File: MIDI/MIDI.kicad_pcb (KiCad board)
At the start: 2 copper layers, 85.8 x 137 mm, 136 parts, among them J1 DIN_5, J2 DIN_5, J3 DIN_5, J4 CONN_01X06, J5 CONN_01X06, SW1 SW_PUSH, SW10 SW_PUSH, SW11 SW_PUSH, SW12 SW_PUSH, SW2 SW_PUSH, SW3 SW_PUSH, SW4 SW_PUSH, SW5 SW_PUSH, SW6 SW_PUSH, SW7 SW_PUSH, SW8 SW_PUSH, SW9 SW_PUSH, U1 6N138, U2 4050, U3 40106, U4 ENCODER_w_SWITCH, U5 ENCODER_w_SWITCH, U6 ENCODER_w_SWITCH

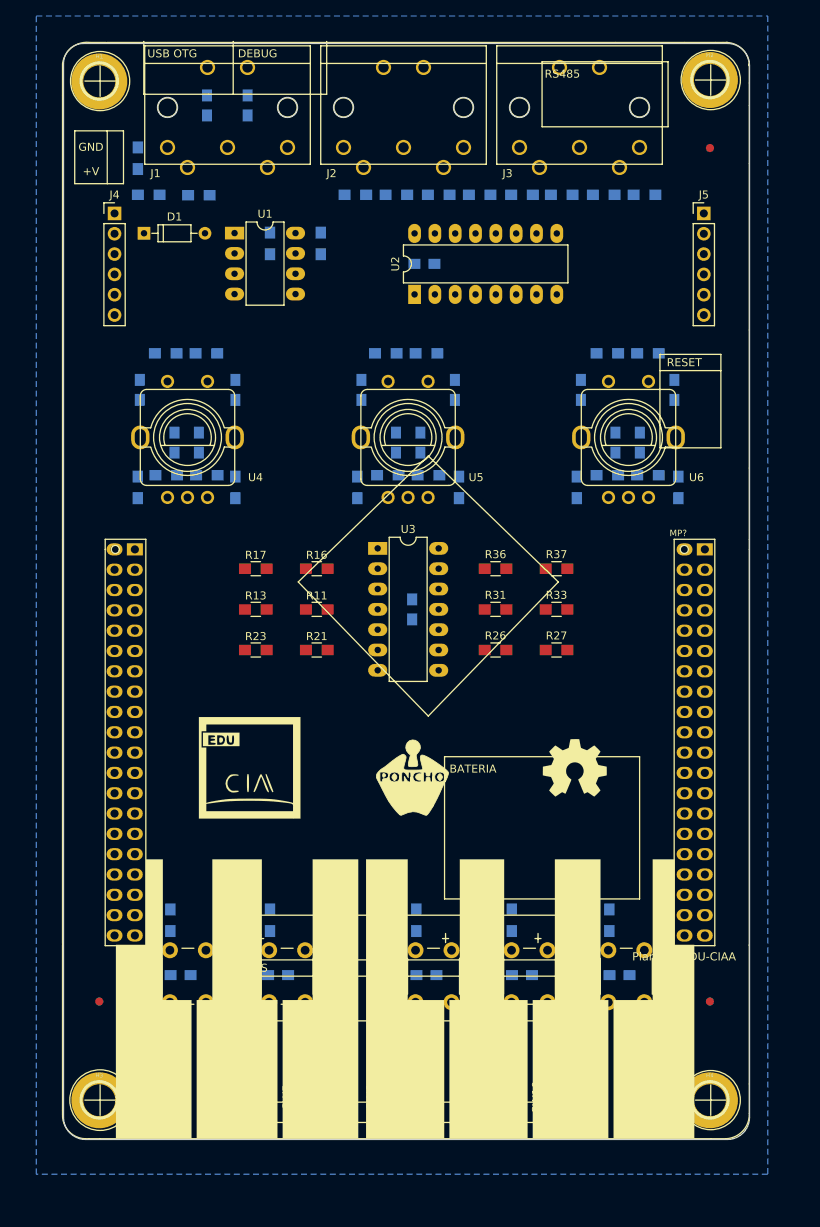
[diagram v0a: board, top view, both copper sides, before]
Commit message: Se comienza a realizar una primer iteración de ruteo
> Se trazan algunas líneas para estudiar si el placement es adecuado.
> Se realizan pequeñas modificaciones en la posición de componentes accesorios para facilitar el ruteo.
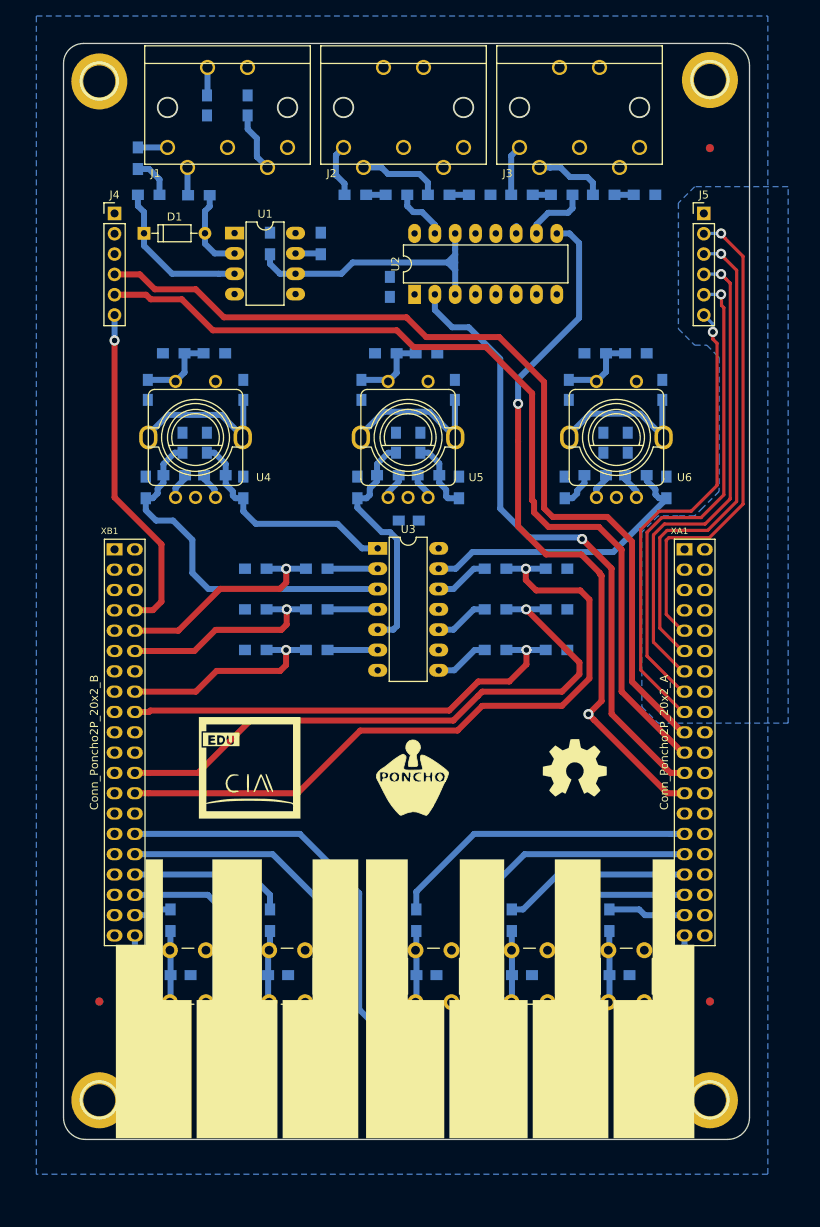
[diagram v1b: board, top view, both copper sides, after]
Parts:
- removed MP?: Plantilla_EDU-CIAA, MIDI:Plantilla_EDU-CIAA
- R11, R13, R16, R17, R21, R23, R26, R27, R31, R33, R36, R37: moved to B.Cu
- XA1, XB1: moved to F.Cu
- moved C16 11.1 mm to (84.7, 83.4), turned to 180 degrees
- moved C3 5.19 mm to (82.3, 54.2), turned to 270 degrees
- moved R47 1.78 mm to (83.6, 148.6)
- moved R51 1.78 mm to (81.8, 148.6)
- moved R53 1.78 mm to (92.2, 148.6)
- moved R49 1.75 mm to (94.0, 148.6)
- moved R29 1.51 mm to (116.9, 79.2)
- moved R30 1.51 mm to (108.0, 62.5)
- moved R32 1.51 mm to (108.0, 77.7)
- moved U6 1.51 mm to (110.6, 73.0)
- moved C12 1.51 mm to (104.7, 67.1)
- moved C13 1.51 mm to (109.0, 73.7)
- moved C14 1.51 mm to (112.0, 73.7)
- moved C15 1.51 mm to (116.3, 67.1)
- moved R28 1.51 mm to (104.2, 79.2)
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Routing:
- net /Conectores/I2C_SDA: track 0.00 -> 114.5 mm
- net /Conectores/I2C_SCL: track 0.00 -> 113.9 mm
- net /Interfaz MIDI/TX-UART: track 0.00 -> 89.0 mm, vias 0 -> 2
- net /Conectores/ENC_B2: track 0.00 -> 87.9 mm, vias 0 -> 1
- net /Interfaz MIDI/RX-UART: track 0.00 -> 78.7 mm, vias 0 -> 1
- net /Conectores/ENC_A2: track 0.00 -> 76.5 mm, vias 0 -> 1
- net /Conectores/ADC3: track 0.00 -> 61.4 mm, vias 0 -> 1
- net /Conectores/ADC1: track 0.68 -> 61.7 mm, vias 0 -> 1
- net /Conectores/ADC2: track 0.00 -> 60.9 mm, vias 0 -> 1
- net /Conectores/DAC: track 0.00 -> 60.8 mm, vias 0 -> 1
- net /Conectores/VDDA: track 0.00 -> 59.0 mm, vias 0 -> 1
- net /Conectores/ENC_B1: track 0.00 -> 58.1 mm, vias 0 -> 1
- net /Conectores/PUL5: track 0.00 -> 50.1 mm
- net Net-(C5-Pad1): track 0.00 -> 45.7 mm
- net /Conectores/PUL7: track 0.00 -> 45.0 mm
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- added copper zone on B.Cu, net /Conectores/GNDA
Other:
- net class Angosto added: clearance 0.4, trace_width 0.4, via_dia 1.27, via_drill 0.7
- net class Default: clearance 0.2 -> 0.5; trace_width 0.25 -> 0.75; via_dia 0.6 -> 1.27; via_drill 0.4 -> 0.7
- rule trace_clearance: 0.2 -> 0.5
- rule trace_min: 0.2 -> 0.3
- rule via_min_drill: 0.3 -> 0.7
- rule via_min_size: 0.4 -> 1.27
- board text added: "0,2540mm (10mils) 0,30mm 1,27mm 0,70mm MIXED MIXED HASL"
- board text added: "Grilas - Posicionamiento: - Ruteo: Valores mínimos - Pista: - Vía: - Agujero Vía: Capas - Top: - Bottom: Terminación superficial:"

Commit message: Se avanza con primera iteración de ruteo
> Se terminan de rutear conexiones para estudiar factibilidad de placement.
> Para facilitar el ruteo se realizan los siguientes cambios:
  > Se desconecta pin redundante de tact-switch's para permitir la conexión entre planos de masa.
  > Se desconectan pines del conector derecho de forma que no requieran ser ruteados a los homologos del conector izquierdo.
  > Se intercambian unidades F y D del componente 40106.
  > Se agrupan señales de los interruptores de los encoders en vez de intercalarlos con las señales de encoder, propiamente dicho, de cada uno. Se rutean a pines superiores en el conector izquierdo, mientras se desplazan las restantes señales hacia abajo.

> Se aguarda comentarios de los revisores para emprolijar, embellecer y mejorar el ruteo.
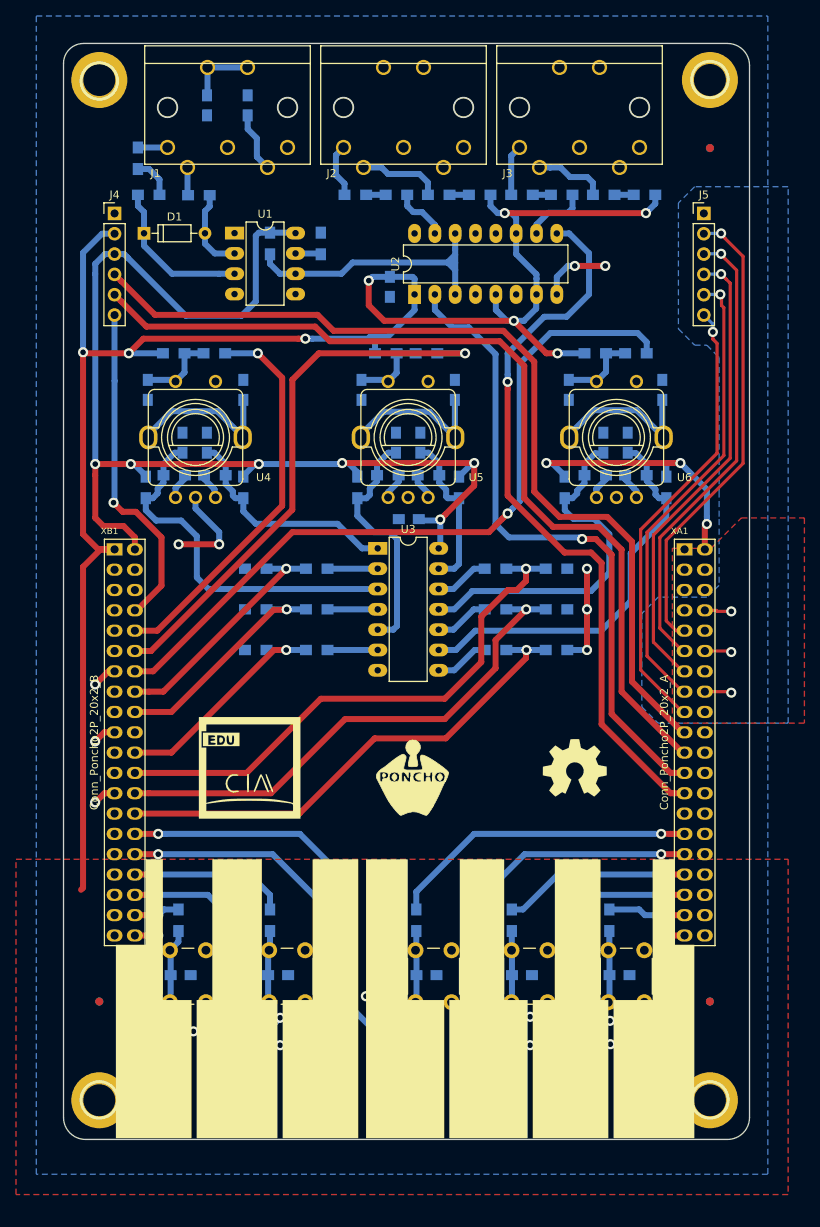
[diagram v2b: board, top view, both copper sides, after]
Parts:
- moved R26 10.2 mm to (95.5, 89.4)
- moved R27 10.2 mm to (103.1, 89.4)
- moved R36 10.2 mm to (95.5, 99.6)
- moved R37 10.2 mm to (103.1, 99.6)
- moved R43 1.00 mm to (55.9, 133.3)
- moved R39 0.51 mm to (51.6, 143.3)
- moved R42 0.20 mm to (49.8, 148.6)
- moved R53 0.20 mm to (92.0, 148.6)
- moved C16 0.18 mm to (84.7, 83.2)
- moved R50 0.15 mm to (73.3, 148.6)
- moved R51 0.15 mm to (81.6, 148.6)
- moved R61 0.15 mm to (114.7, 148.6)
- moved R55 0.10 mm to (102.3, 148.6)
- moved R41 0.05 mm to (64.5, 144.8)
- moved R40 0.05 mm to (62.5, 148.6)
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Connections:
- SW10 pad 1: Net-(C26-Pad1) -> Net-(SW10-Pad1)
- SW12 pad 1: Net-(C28-Pad1) -> Net-(SW12-Pad1)
- SW3 pad 1: Net-(C19-Pad1) -> Net-(SW3-Pad1)
- SW5 pad 1: Net-(C21-Pad1) -> Net-(SW5-Pad1)
- SW6 pad 1: Net-(C22-Pad1) -> Net-(SW6-Pad1)
- SW8 pad 1: Net-(C24-Pad1) -> Net-(SW8-Pad1)
- U3 pad 12: Net-(R36-Pad2) -> Net-(R26-Pad2)
- U3 pad 13: Net-(C14-Pad1) -> Net-(C10-Pad1)
- U3 pad 8: Net-(R26-Pad2) -> Net-(R36-Pad2)
- U3 pad 9: Net-(C10-Pad1) -> Net-(C14-Pad1)
- XA1 pad 1: +3.3V -> Net-(XA1-Pad1)
- XA1 pad 4: GND -> Net-(XA1-Pad4)
- XB1 pad 10: /Conectores/ENC_B0 -> /Conectores/ENC_SW0
- XB1 pad 12: /Conectores/ENC_A0 -> /Conectores/ENC_SW1
- XB1 pad 14: /Conectores/ENC_SW0 -> /Conectores/ENC_SW2
- XB1 pad 16: /Conectores/ENC_A1 -> /Conectores/ENC_B0
- XB1 pad 18: /Conectores/ENC_B1 -> /Conectores/ENC_A0
- XB1 pad 22: /Conectores/ENC_SW1 -> /Conectores/ENC_A1
- XB1 pad 24: /Conectores/ENC_A2 -> /Conectores/ENC_B1
- XB1 pad 26: /Conectores/ENC_B2 -> /Conectores/ENC_A2
- XB1 pad 28: /Conectores/ENC_SW2 -> /Conectores/ENC_B2
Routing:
- net +3.3V: track 0.95 -> 274.0 mm, vias 0 -> 16
- net +5V: track 0.00 -> 186.2 mm, vias 0 -> 9
- net /Conectores/ENC_SW2: track 0.00 -> 93.4 mm, vias 0 -> 1
- net /Conectores/ENC_SW1: track 0.00 -> 69.7 mm, vias 0 -> 1
- net /Conectores/ENC_SW0: track 0.00 -> 49.3 mm, vias 0 -> 1
- net GND: track 0.00 -> 42.1 mm, vias 0 -> 10
- net Net-(C13-Pad1): track 4.45 -> 45.2 mm
- net /Conectores/ENC_B2: track 87.9 -> 63.1 mm
- net Net-(C14-Pad1): track 36.6 -> 50.0 mm
- net /Conectores/ENC_A2: track 76.5 -> 65.5 mm
- net Net-(C10-Pad1): track 9.11 -> 20.1 mm
- net /Conectores/ENC_B1: track 58.1 -> 68.6 mm
- net /Conectores/GNDA: track 0.00 -> 10.1 mm, vias 0 -> 3
- net /Conectores/PUL0: track 12.5 -> 17.6 mm, vias 0 -> 1
- net Net-(C1-Pad1): track 3.52 -> 8.52 mm
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- added copper zone on F.Cu, net +3.3V
- added copper zone on F.Cu, net /Conectores/GNDA
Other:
- board text added: "0,2540mm (10mils) 0,1270/0,2540mm (5/10mils) 0,30mm 1,27mm (50mils) 0,70mm MIXED MIXED HASL"
- board text added: "Grilas - Posicionamiento: - Ruteo: Valores mínimos - Pista: - Vía: - Orificio Vía: Capas - Top: - Bottom: Terminación superficial:"
- board text removed: "0,2540mm (10mils) 0,30mm 1,27mm 0,70mm MIXED MIXED HASL"
- board text removed: "Grilas - Posicionamiento: - Ruteo: Valores mínimos - Pista: - Vía: - Agujero Vía: Capas - Top: - Bottom: Terminación superficial:"

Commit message: Correciones menores
> Se elimina nombre de componentes ( tiras de pines ) de la capa de serigrafía.
> Se realizan correciones menores al ruteo y se agregan vías para conectar plano de masa en capa bottom y conector derecho en capa front.
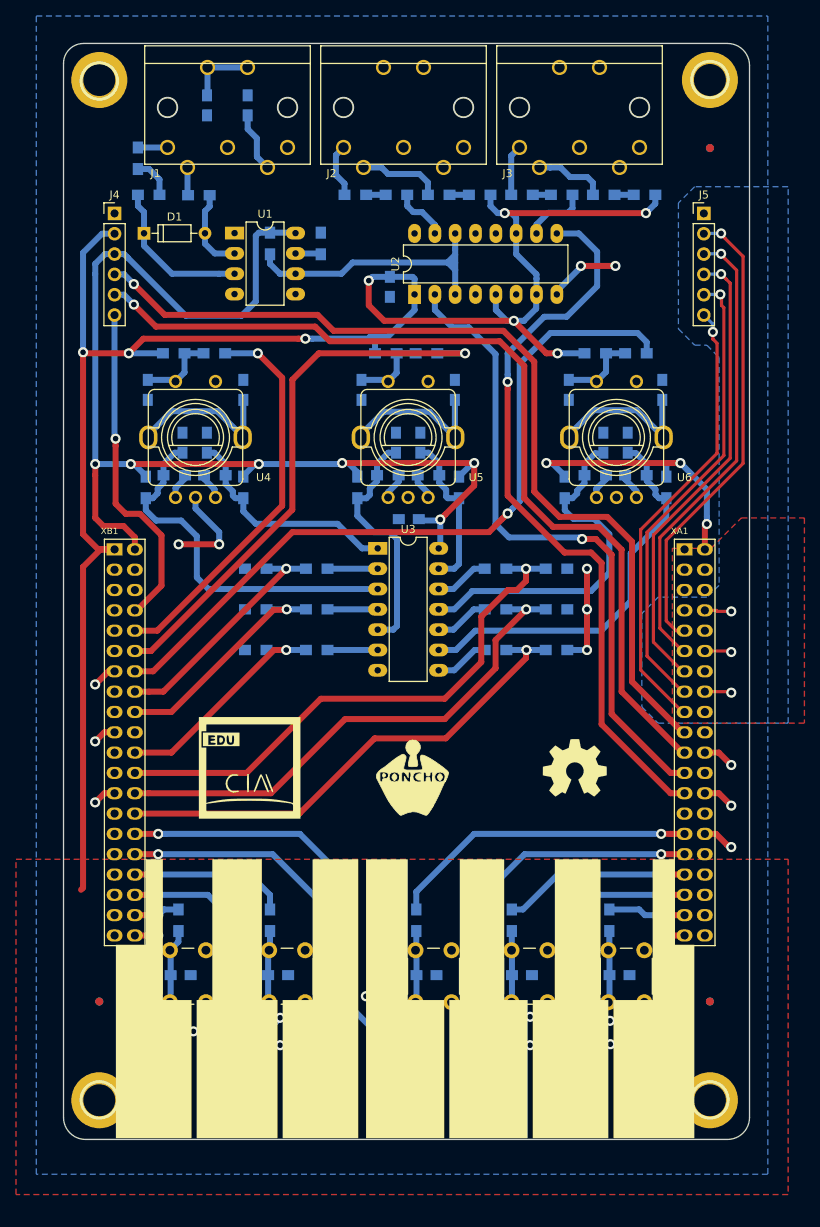
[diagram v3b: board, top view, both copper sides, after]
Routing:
- net GND: track 42.1 -> 54.1 mm, vias 10 -> 13
- net /Interfaz MIDI/TX-UART: track 90.5 -> 92.1 mm
- net /Conectores/I2C_SCL: vias 0 -> 1
- net /Conectores/I2C_SDA: vias 0 -> 1

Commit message: Se realizan cambios según revisiones
> Se realizan diversos cambios detallados en los respectivos archivos de revision (Moreno y Brengi 2da.) presentes en /Doc/Revisiones/.
> Se genera la versión 0.9 del circuito.
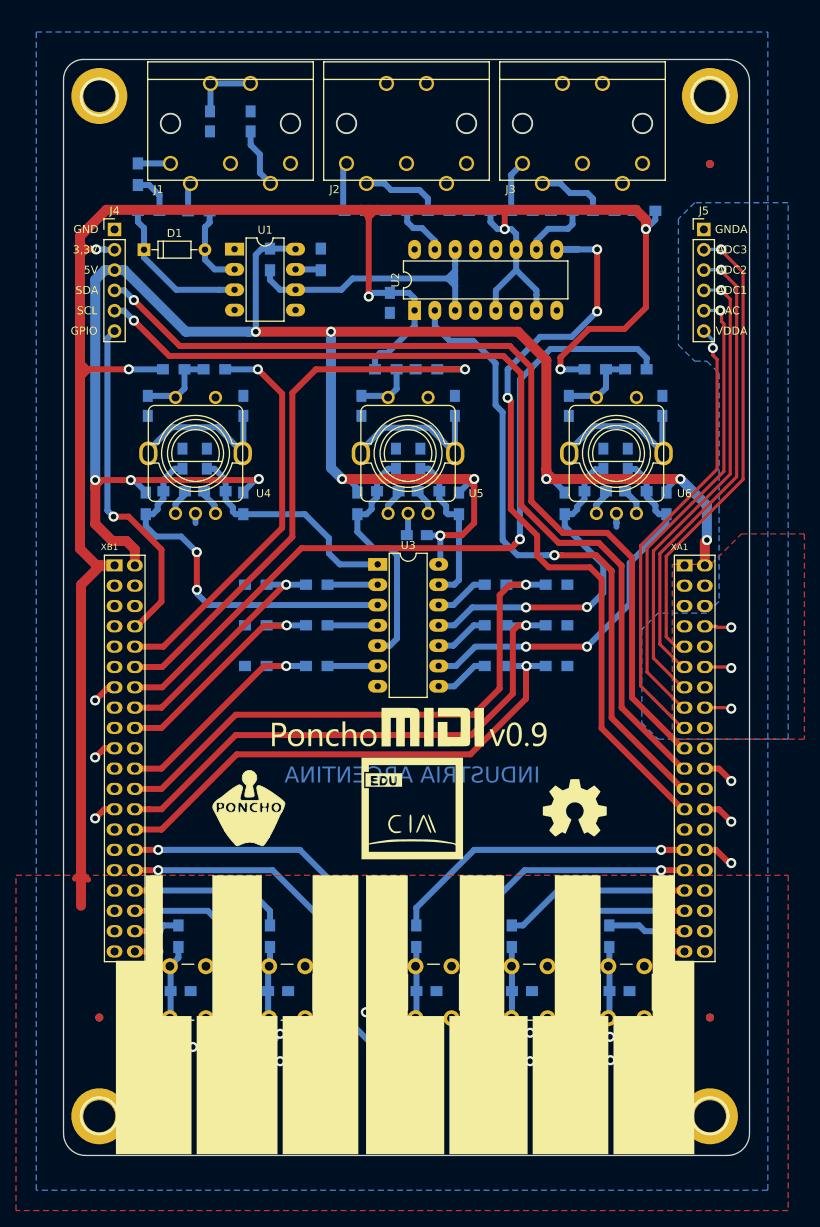
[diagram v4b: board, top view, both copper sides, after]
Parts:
- added G***: LOGO, MIDI:nombrePoncho, F.Cu at (84.7, 109.2)
- moved G1 20.9 mm to (85.1, 119.4)
- moved G2 20.8 mm to (64.6, 119.4)
- moved SW1 6.26 mm to (54.9, 154.3), turned to 270 degrees
- moved G3 5.00 mm to (105.4, 119.3)
- moved R38 4.47 mm to (55.8, 150.6)
- moved R42 4.47 mm to (53.8, 150.6)
- moved C17 2.69 mm to (53.7, 157.6), turned to 180 degrees
- moved C16 2.24 mm to (85.7, 85.2)
- moved D1 2.05 mm to (51.6, 49.5)
- moved C1 2.03 mm to (59.8, 33.5)
- moved C2 2.03 mm to (64.9, 33.5)
- moved J1 2.03 mm to (62.4, 35.0)
- moved J2 2.03 mm to (84.4, 35.0)
- moved J3 2.03 mm to (106.4, 35.0)
- moved C10 2.00 mm to (86.1, 75.7)
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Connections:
- net /Conectores/GNDA renamed GNDA
- SW1 pad 2: Net-(C17-Pad1) -> Net-(SW1-Pad2)
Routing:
- net +5V: track 186.2 -> 252.7 mm, vias 9 -> 11
- net +3.3V: track 274.0 -> 318.9 mm, vias 16 -> 14
- net GND: track 54.1 -> 26.2 mm, vias 13 -> 6
- net /Interfaz MIDI/TX-UART: track 92.1 -> 97.0 mm, vias 1 -> 3
- net /Conectores/PUL0: track 17.6 -> 21.1 mm
- net Net-(C17-Pad1): track 11.0 -> 8.01 mm
- net /Conectores/ENC_B1: track 68.6 -> 71.2 mm
- net /Conectores/ENC_A2: track 65.5 -> 68.0 mm
- net Net-(C13-Pad1): track 45.2 -> 42.8 mm, vias 0 -> 2
- net /Conectores/ENC_B2: track 63.1 -> 64.9 mm
- net /Conectores/ENC_SW2: track 93.4 -> 95.1 mm
- net Net-(C14-Pad1): track 50.0 -> 49.0 mm, vias 0 -> 2
- net /Conectores/ENC_SW1: track 69.7 -> 70.7 mm
- net Net-(J4-Pad6): track 41.9 -> 42.7 mm
- net Net-(FB4-Pad2): track 6.80 -> 6.17 mm
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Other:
- outline, holes or cut-outs redrawn
- board text added: "3,3V"
- board text added: "5V"
- board text added: "ADC1"
- board text added: "ADC2"
- board text added: "ADC3"
- board text added: "DAC"
- board text added: "GND"
- board text added: "GNDA"
- board text added: "GPIO"
- board text added: "Grillas - Posicionamiento: - Ruteo: Valores mínimos - Pista: - Vía: - Orificio Vía: Capas - Top: - Bottom: Terminación superficial:"
- board text added: "INDUSTRIA ARGENTINA"
- board text added: "SCL"
- board text added: "SDA"
- board text added: "VDDA"
- board text removed: "Grilas - Posicionamiento: - Ruteo: Valores mínimos - Pista: - Vía: - Orificio Vía: Capas - Top: - Bottom: Terminación superficial:"
